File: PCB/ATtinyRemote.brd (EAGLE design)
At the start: 49.2 x 26.7 mm, 14 parts, among them IC1 ATTINY85DIP8, Q1 BC547, Q2 16MHz, U1 IR_Emitter, U2 IR_Receiver, X1 USB-A-H

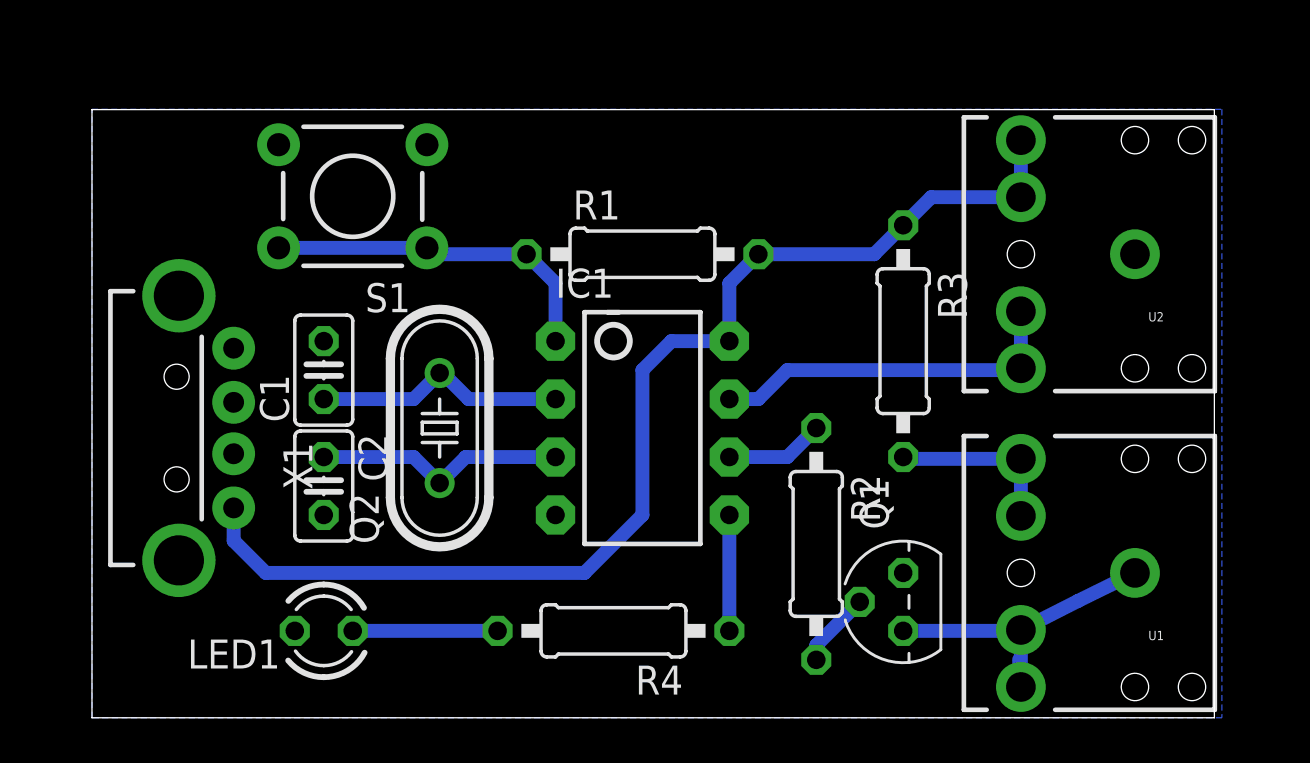
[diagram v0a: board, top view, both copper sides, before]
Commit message: Minor adjustments to make it work better in practice
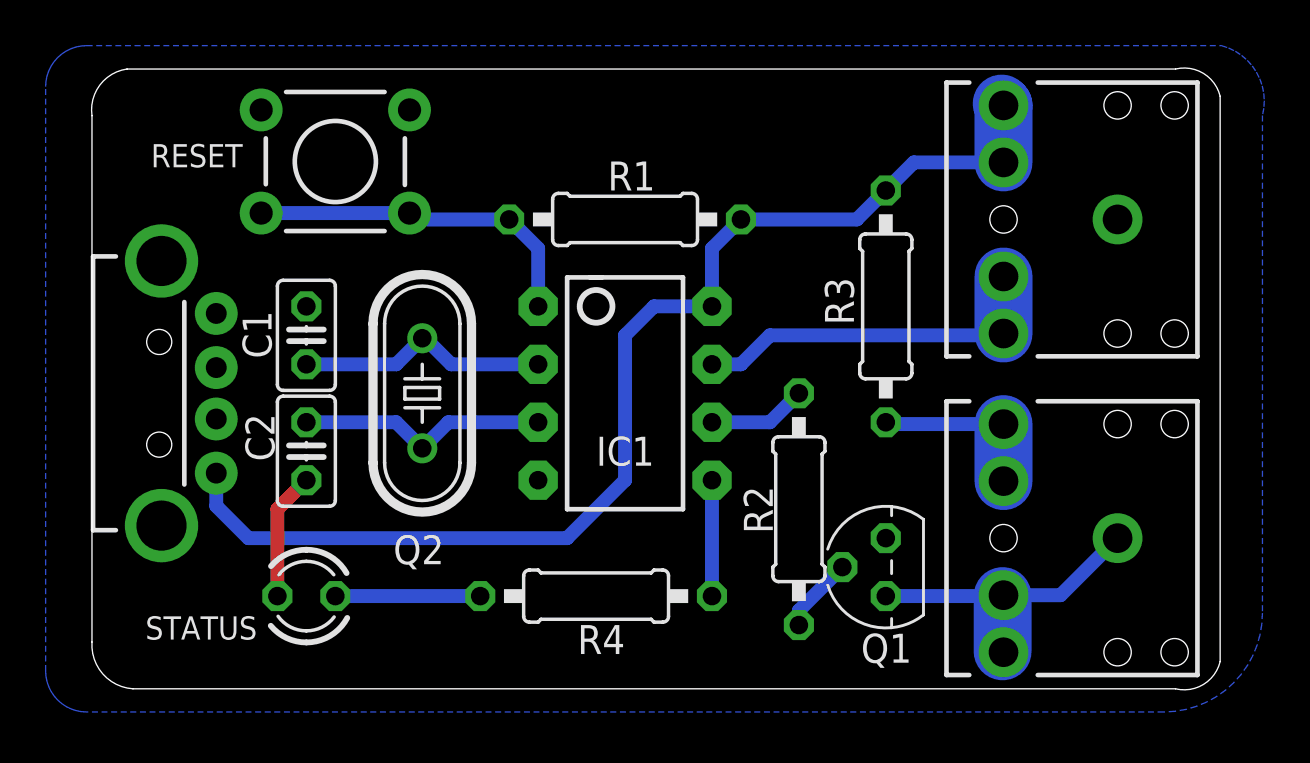
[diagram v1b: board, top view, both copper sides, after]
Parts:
- removed LED1: (no value), led:LED3MM
- removed S1: RESET, SparkFun:TACTILE-PTH
- added RESET: RESET, SparkFun:TACTILE-PTH
- added STATUS: (no value), led:LED3MM
- moved IC1 1.70 mm to (23.4, 13.0)
- moved Q2 1.70 mm to (14.5, 13.0)
- moved R1 1.70 mm to (23.4, 20.6)
- moved U2 1.70 mm to (45.0, 20.6)
- moved X1 1.70 mm to (3.05, 13.0)
- moved R2 1.70 mm to (31.0, 7.87)
- moved R4 1.70 mm to (22.1, 4.06)
- moved U1 1.70 mm to (45.0, 6.60)
- moved Q1 1.70 mm to (34.8, 5.33)
- moved C1 1.70 mm to (9.40, 15.5)
- moved C2 1.70 mm to (9.40, 10.4)
- moved R3 1.70 mm to (34.8, 16.8)
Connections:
- net GND: now also RESET.3, RESET.4, STATUS.K; no longer LED1.K, S1.3, S1.4
- net N$3: now also RESET.1, RESET.2; no longer S1.1, S1.2
- net N$9: now also STATUS.A; no longer LED1.A
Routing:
- net GND: track 0.00 -> 5.61 mm
- net N$5: track 14.5 -> 13.6 mm
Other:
- board size 49.2 x 26.7 mm -> 49.5 x 27.3 mm
- board text added: "ATtinyRemote"
- board text added: "ATtinyRemote V1.0"
- board text added: "C"
- board text added: "Emitter"
- board text added: "Receiver"
- board text added: "TKJ Electronics 2012"
